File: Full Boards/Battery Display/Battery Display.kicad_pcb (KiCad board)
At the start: 4 copper layers, 110 x 175.2 mm, 195 parts, among them J3 Program Header, J4 Optional Bond, Q10 DMN6075S, Q11 BSS314PE, Q12 DMN6075S, Q7 BSS314PE, Q8 DMN6075S, Q9 BSS314PE, SW3 Boot, SW4 Reset

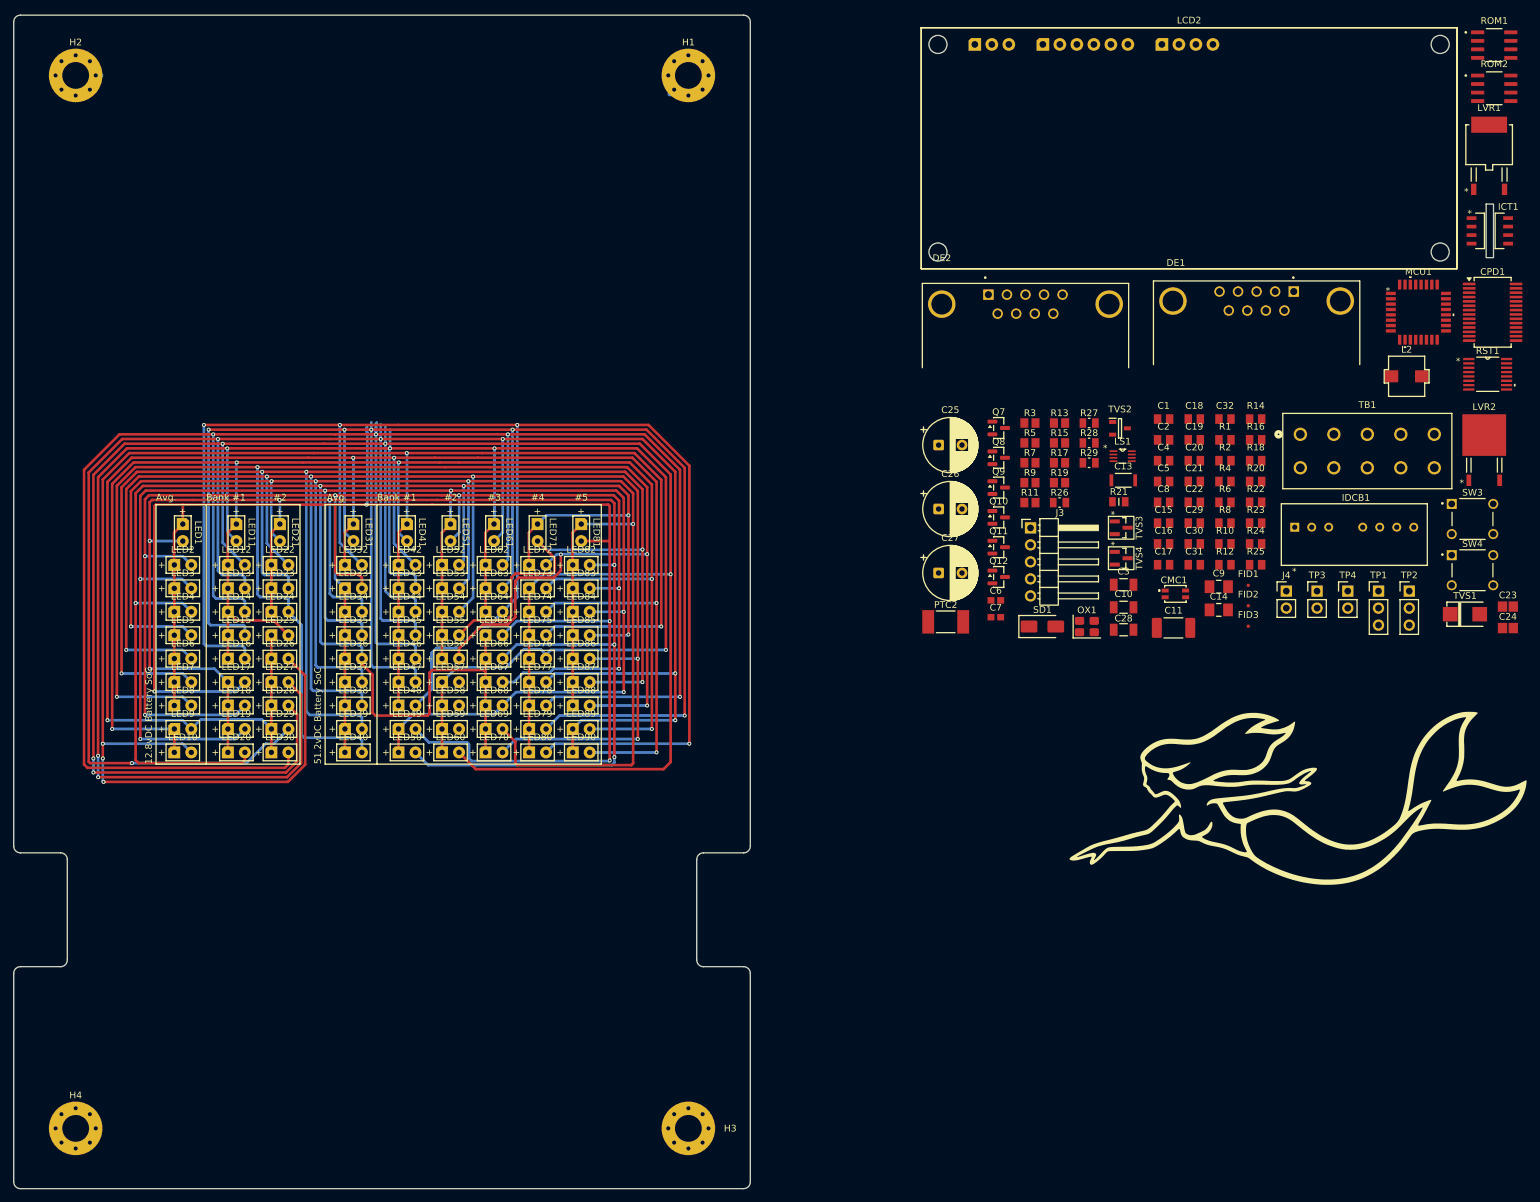
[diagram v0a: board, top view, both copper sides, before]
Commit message: Finished layout of the battery display PCB. Updated the silkscreen on the Compass Rose as well.
Signed-off-by: digimer <digital.mermaid@gmail.com>
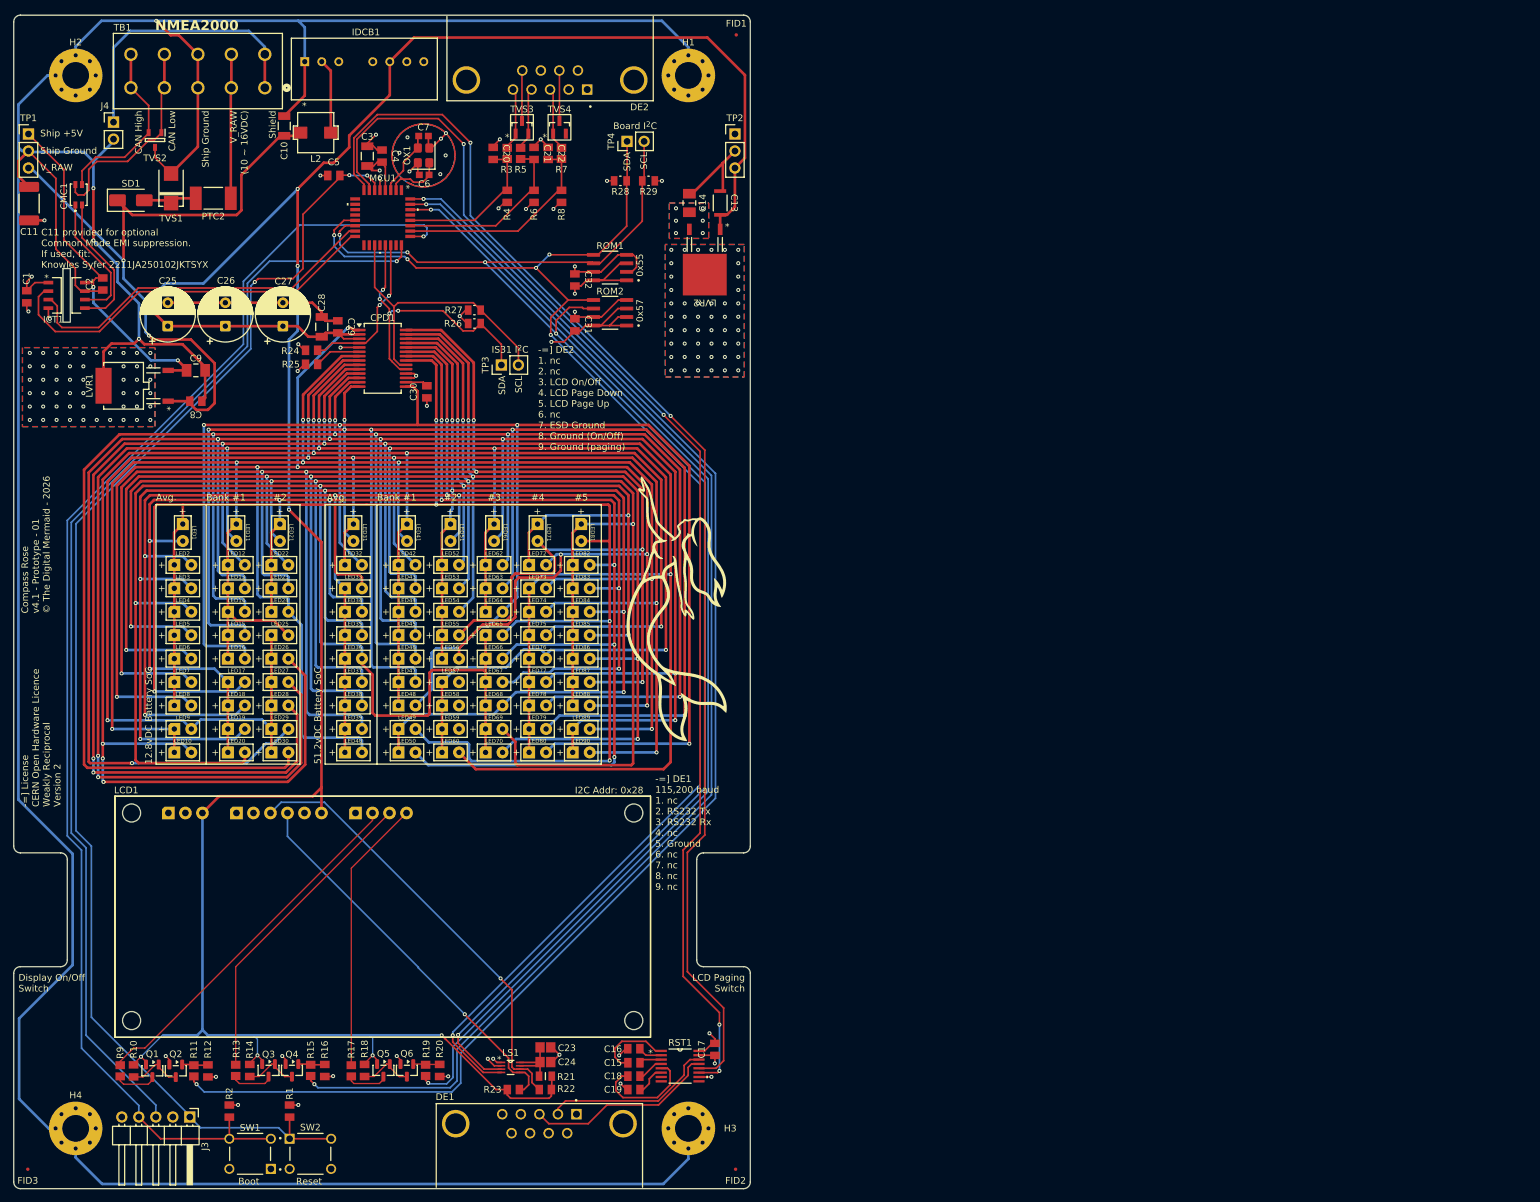
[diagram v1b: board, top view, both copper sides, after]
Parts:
- DE2: footprint mr-stuff:Amphenol_L777SDE09PA4CH4F -> mr-stuff:Amphenol L777SDE09PA4CH4F
- TDM***: footprint mr-stuff:Mermaid Silkscreen - 29.9mm -> mr-stuff:Mermaid Silkscreen - 15mm
- moved TP1 212.9 mm to (47.1, 37.5)
- moved ICT1 212.8 mm to (52.8, 61.6)
- moved LVR1 207.1 mm to (61.3, 75.1), turned to 90 degrees
- moved SW1 205.7 mm to (80.2, 189.8), turned to 180 degrees
- moved TB1 204.2 mm to (62.4, 25.6), turned to 180 degrees
- moved TVS1 203.4 mm to (68.4, 45.6), turned to 90 degrees
- moved FID3 199.5 mm to (47.0, 192.1), turned to 180 degrees
- moved SW2 194.2 mm to (89.2, 189.8)
- moved J4 188.6 mm to (59.8, 35.7)
- moved C11 182.3 mm to (47.2, 47.9), turned to -90 degrees
- moved R10 181.0 mm to (62.8, 177.4), turned to 90 degrees
- moved R14 179.0 mm to (80.2, 177.3), turned to 90 degrees
- moved R2 177.6 mm to (77.1, 183.4), turned to 90 degrees
- moved CMC1 174.0 mm to (54.6, 46.8), turned to 90 degrees
- moved R1 171.9 mm to (86.1, 183.4), turned to 90 degrees
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- renumbered LCD2 to LCD1, Q7 to Q1, Q8 to Q2, Q9 to Q3, Q10 to Q4, Q11 to Q5, Q12 to Q6, SW3 to SW1, SW4 to SW2
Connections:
- R24 pad 1: /IS31_INTB_OUT -> +3.3V
- R24 pad 2: +3.3V -> /IS31_INTB_OUT
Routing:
- net GND_SHIP: track 8.02 -> 537.8 mm, vias 0 -> 56
- net +5V: track 0.00 -> 406.4 mm, vias 0 -> 8
- net /BOARD_I2C_SCL: track 0.00 -> 227.2 mm, vias 0 -> 5
- net /BOARD_I2C_SDA: track 0.00 -> 221.9 mm, vias 0 -> 6
- net /LCD_BL_RED_OUT: track 0.00 -> 211.2 mm, vias 0 -> 2
- net /DEBUG_SWCLK: track 0.00 -> 199.1 mm, vias 0 -> 1
- net /NRST: track 0.00 -> 198.9 mm, vias 0 -> 3
- net /LCD_BL_GREEN_OUT: track 0.00 -> 191.3 mm, vias 0 -> 2
- net /USART1_RX: track 0.00 -> 188.1 mm, vias 0 -> 2
- net /USART1_TX: track 0.00 -> 186.6 mm, vias 0 -> 4
- net /LCD_BL_BLUE_OUT: track 0.00 -> 171.7 mm, vias 0 -> 2
- net /DEBUG_SWDIO: track 0.00 -> 167.0 mm, vias 0 -> 1
- net GND: track 0.00 -> 130.7 mm, vias 0 -> 80
- net V_RAW: track 0.00 -> 102.1 mm, vias 0 -> 2
- net +3.3V: track 0.00 -> 73.4 mm, vias 0 -> 22
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- added copper zone on B.Cu, net +3.3V
- added copper zone on F.Cu, net +3.3V
- added copper zone on B.Cu, net GND
- added copper zone on F.Cu, net GND
- added copper zone on In2.Cu, net GND
- added copper zone on B.Cu, net GND_SHIP
- added copper zone on F.Cu, net GND_SHIP
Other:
- board text added: "-=] DE1 115,200 baud 1. nc 2. RS232 Tx 3. RS232 Rx 4. nc 5. Ground 6. nc 7. nc 8. nc 9. nc"
- board text added: "-=] DE2 1. nc 2. nc 3. LCD On/Off 4. LCD Page Down 5. LCD Page Up 6. nc 7. ESD Ground 8. Ground (On/Off) 9. Ground (paging)"
- board text added: "-=] License CERN Open Hardware Licence Weakly Reciprocal Version 2"
- board text added: "0x55"
- board text added: "0x57"
- board text added: "Board I^{2}C"
- board text added: "Boot"
- board text added: "C11 provided for optional Common Mode EMI suppression. If used, fit: Knowles Syfer 2211JA250102JKTSYX"
- board text added: "CAN High"
- board text added: "CAN Low"
- board text added: "Compass Rose v4.1 - Prototype - 01 © The Digital Mermaid - 2026"
- board text added: "Display On/Off Switch"
- board text added: "I2C Addr: 0x28"
- board text added: "IS31 I^{2}C"
- board text added: "LCD Paging Switch"
- board text added: "NMEA2000"
- board text added: "Reset"
- board text added: "SCL"
- board text added: "SDA"
- board text added: "Shield"
- board text added: "Ship +5V"
- board text added: "Ship Ground"
- board text added: "V_RAW"
- board text added: "V_RAW (10 ~ 16VDC)"

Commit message: Moved traces from In1.Cu (GND) to In2.Cu (+3.3V).
Signed-off-by: digimer <digital.mermaid@gmail.com>
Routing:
- net /CB1: track 294.2 -> 295.1 mm
- net /CB2: track 308.6 -> 309.2 mm
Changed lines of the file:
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@@
 	)
 	(segment
+		(start 141.596496 175.074999)
+		(end 139.292595 175.074999)
+		(width 0.254)
+		(layer "F.Cu")
+		(net "Net-(RST1-VS+)")
+	)
+	(segment
+		(start 139.292595 175.074999)
+		(end 138.417596 174.2)
+		(width 0.254)
+		(layer "F.Cu")
+		(net "Net-(RST1-VS+)")
+	)
+	(segment
 		(start 78.05 178.75)
 		(end 78.6 179.3)
@@
 	)
 	(segment
-		(start 111.4 119.35255)
-		(end 109.84745 117.8)
+		(start 104.49255 98.29255)
+		(end 103.63 98.29255)
 		(width 0.4)
-		(layer "In1.Cu")
+		(layer "In2.Cu")
 		(net "/CB1")
 	)
 	(segment
-		(start 109.84745 117.8)
-		(end 107.1 117.8)
+		(start 111.4 118.4)
+		(end 110.6 117.6)
 		(width 0.4)
-		(layer "In1.Cu")
+		(layer "In2.Cu")
 		(net "/CB1")
 	)
 	(segment
-		(start 107.1 117.8)
-		(end 106.4 117.1)
+		(start 106.9 117.2)
+		(end 106.9 100.7)
 		(width 0.4)
-		(layer "In1.Cu")
+		(layer "In2.Cu")
 		(net "/CB1")
 	)
 	(segment
-		(start 106.4 117.1)
-		(end 106.4 101.06255)
+		(start 106.9 100.7)
+		(end 104.49255 98.29255)
 		(width 0.4)
-		(layer "In1.Cu")
+		(layer "In2.Cu")
 		(net "/CB1")
 	)
 	(segment
-		(start 106.4 101.06255)
-		(end 103.63 98.29255)
+		(start 107.3 117.6)
+		(end 106.9 117.2)
+		(width 0.4)
+		(layer "In2.Cu")
+		(net "/CB1")
+	)
+	(segment
+		(start 111.4 119.35255)
+		(end 111.4 118.4)
 		(width 0.4)
-		(layer "In1.Cu")
+		(layer "In2.Cu")
+		(net "/CB1")
+	)
+	(segment
+		(start 110.6 117.6)
+		(end 107.3 117.6)
+		(width 0.4)
+		(layer "In2.Cu")
 		(net "/CB1")
 	)
@@
 	)
 	(segment
-		(start 130.92 128.92)
-		(end 130.92 129.85255)
-		(width 0.4)
-		(layer "In1.Cu")
-		(net "/CB2")
-	)
-	(segment
-		(start 119.9641 125.6641)
-		(end 119.9641 127.3641)
+		(start 113.4 124.85255)
+		(end 111.4 122.85255)
 		(width 0.4)
-		(layer "In1.Cu")
+		(layer "In2.Cu")
 		(net "/CB2")
 	)
 	(segment
-		(start 111.4 122.85255)
-		(end 113.34745 124.8)
+		(start 113.4 127.7)
+		(end 113.4 124.85255)
 		(width 0.4)
-		(layer "In1.Cu")
+		(layer "In2.Cu")
 		(net "/CB2")
 	)
 	(segment
-		(start 113.34745 124.8)
-		(end 119.1 124.8)
+		(start 130.92 129.02)
+		(end 130 128.1)
 		(width 0.4)
-		(layer "In1.Cu")
+		(layer "In2.Cu")
 		(net "/CB2")
 	)
 	(segment
-		(start 119.9641 127.3641)
-		(end 120.5 127.9)
-		(width 0.4)
-		(layer "In1.Cu")
-		(net "/CB2")
-	)
-	(segment
-		(start 129.9 127.9)
-		(end 130.92 128.92)
+		(start 130.92 129.85255)
+		(end 130.92 129.02)
 		(width 0.4)
-		(layer "In1.Cu")
+		(layer "In2.Cu")
 		(net "/CB2")
 	)
 	(segment
-		(start 119.1 124.8)
-		(end 119.9641 125.6641)
+		(start 130 128.1)
+		(end 113.8 128.1)
 		(width 0.4)
-		(layer "In1.Cu")
+		(layer "In2.Cu")
 		(net "/CB2")
 	)
 	(segment
-		(start 120.5 127.9)
-		(end 129.9 127.9)
+		(start 113.8 128.1)
+		(end 113.4 127.7)
 		(width 0.4)
-		(layer "In1.Cu")
+		(layer "In2.Cu")
 		(net "/CB2")
 	)
@@
 	)
 	(segment
-		(start 104.10745 124.6)
-		(end 102.36 122.85255)
-		(width 0.4)
-		(layer "In1.Cu")
-		(net "/CB3")
-	)
-	(segment
-		(start 110.5 124.6)
+		(start 109.64745 124.6)
 		(end 104.10745 124.6)
 		(width 0.4)
-		(layer "In1.Cu")
+		(layer "In2.Cu")
 		(net "/CB3")
 	)
 	(segment
-		(start 111.4 126.35255)
-		(end 111.4 125.5)
+		(start 104.10745 124.6)
+		(end 102.36 122.85255)
 		(width 0.4)
-		(layer "In1.Cu")
+		(layer "In2.Cu")
 		(net "/CB3")
 	)
 	(segment
-		(start 111.4 125.5)
-		(end 110.5 124.6)
+		(start 111.4 126.35255)
+		(end 109.64745 124.6)
 		(width 0.4)
-		(layer "In1.Cu")
+		(layer "In2.Cu")
 		(net "/CB3")
 	)
@@
 	)
 	(segment
-		(start 141.596496 175.074999)
-		(end 139.292595 175.074999)
-		(width 0.254)
-		(layer "F.Cu")
-		(net "Net-(RST1-VS+)")
-	)
-	(segment
-		(start 139.292595 175.074999)
-		(end 138.417596 174.2)
-		(width 0.254)
-		(layer "F.Cu")
-		(net "Net-(RST1-VS+)")
-	)
-	(segment

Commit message: Fixed Product ID on the Silkscreen.
Signed-off-by: digimer <digital.mermaid@gmail.com>
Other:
- board text added: "Battery Display v4.1 - Prototype - 01 © The Digital Mermaid - 2026"
- board text removed: "Compass Rose v4.1 - Prototype - 01 © The Digital Mermaid - 2026"
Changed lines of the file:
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@@
 		)
 	)
-	(gr_text "Compass Rose\nv4.1 - Prototype - 01\n© The Digital Mermaid - 2026"
+	(gr_text "Battery Display\nv4.1 - Prototype - 01\n© The Digital Mermaid - 2026"
 		(at 46 109.1 90)
 		(layer "F.SilkS")
